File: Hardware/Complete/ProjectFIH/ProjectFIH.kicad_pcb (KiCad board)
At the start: 2 copper layers, 94 x 99.1 mm, 84 parts, among them J1 Conn_01x02_Male, J10 Payload LED, J2 Power, J3 Power LED, J4 MCU Fail LED, J5 Heater LED, J6 Heater, J7 UART, J8 AVR-ISP-10, J9 Payload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

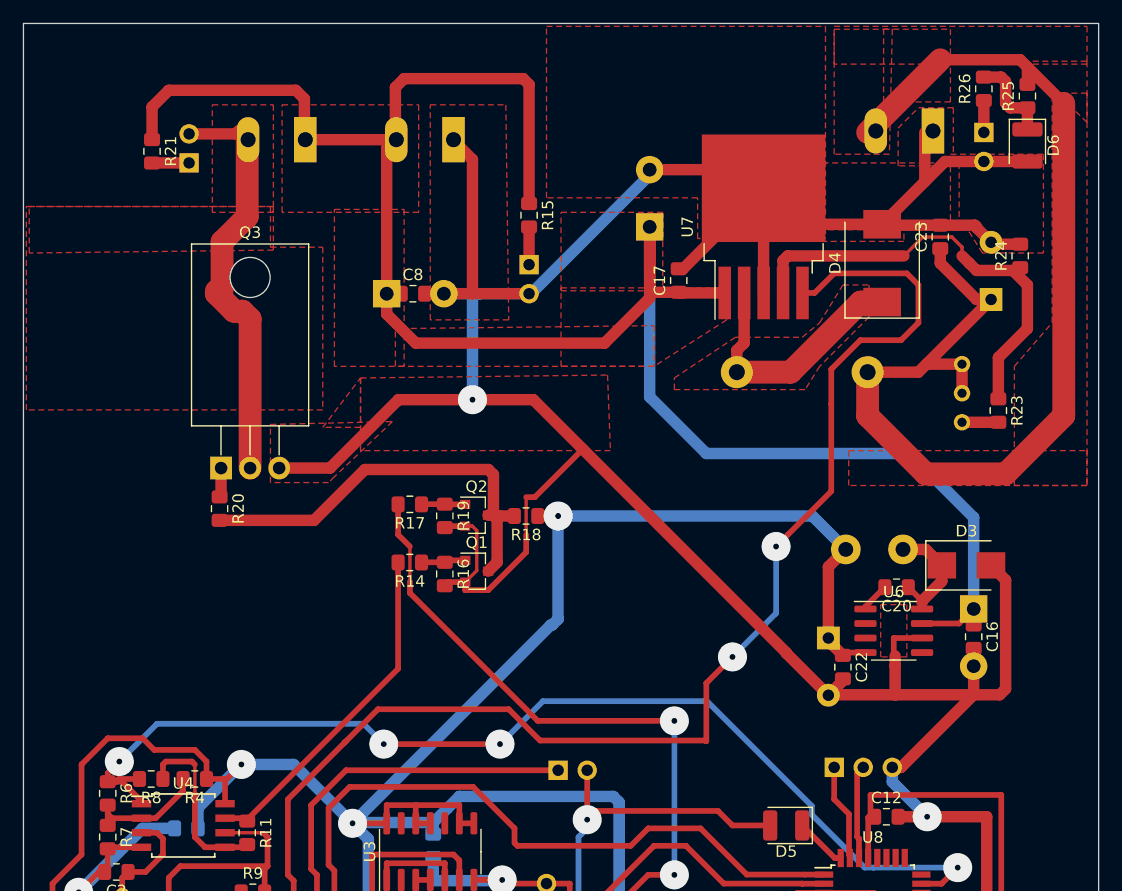
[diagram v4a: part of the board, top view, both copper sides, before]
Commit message: Partially metallized empty spaces.
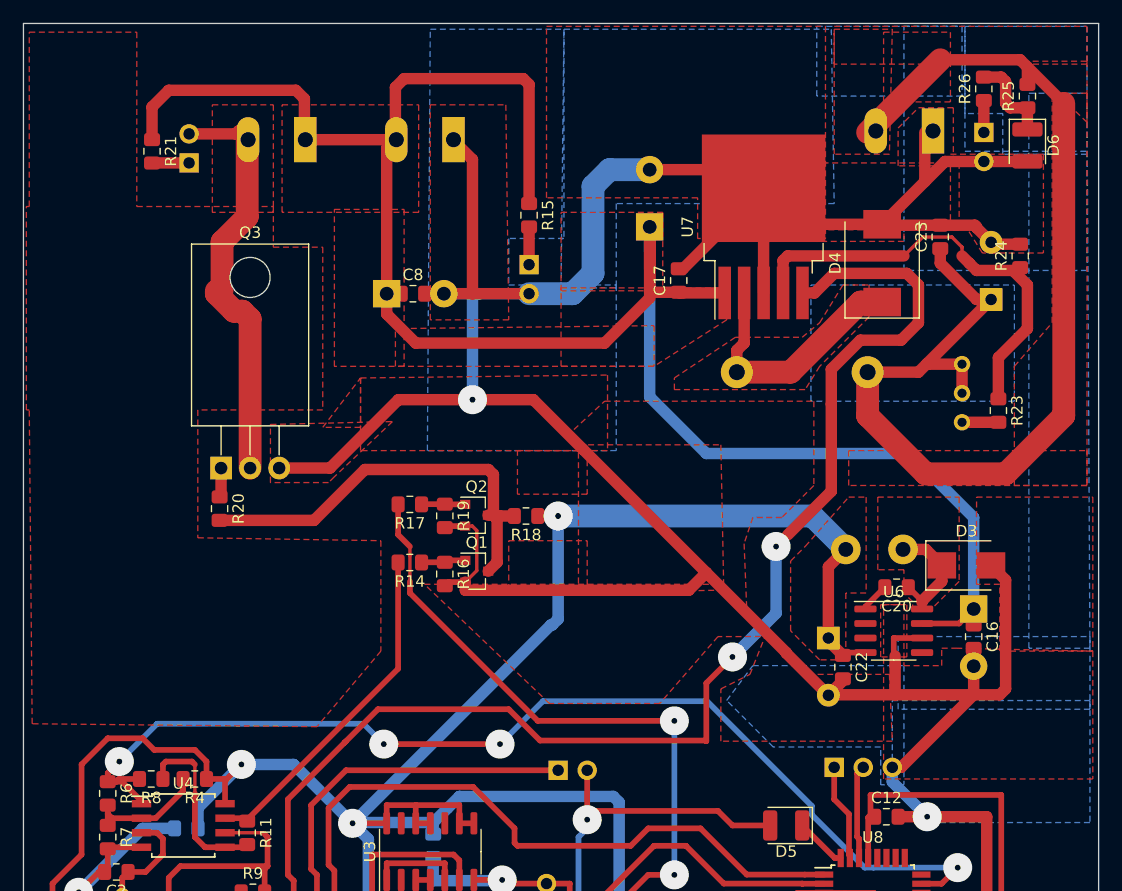
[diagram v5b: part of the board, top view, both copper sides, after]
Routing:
- net GND: track 532.7 -> 541.1 mm
- net +24V: track 178.7 -> 180.8 mm
- added copper zone on F.Cu, net +5V
- added copper zone on B.Cu, net GND
- added copper zone on F.Cu, net Net-(C20-Pad1)
- added copper zone on B.Cu, net Net-(C23-Pad1)

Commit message: Most of metallization
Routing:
- added copper zone on B.Cu, net +24V
- added copper zone on B.Cu, net +5V
- added copper zone on B.Cu, net Net-(J5-Pad2)

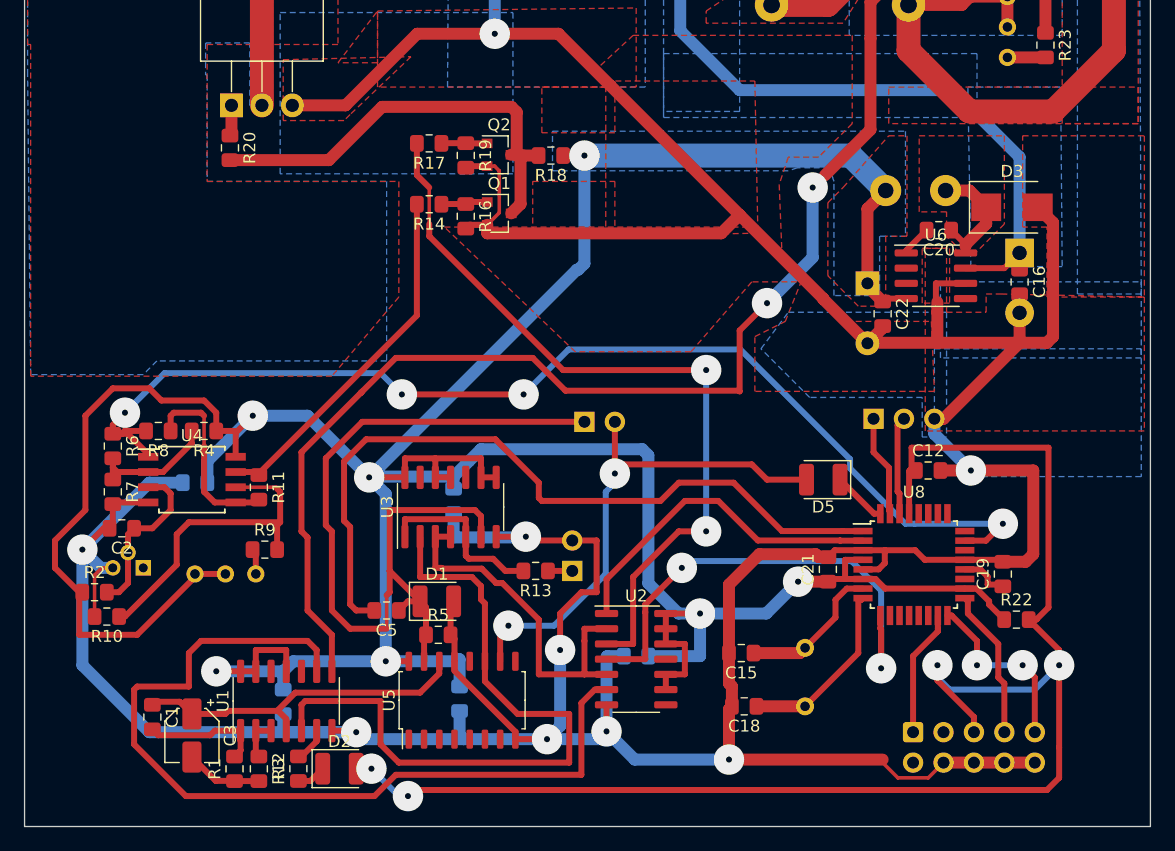
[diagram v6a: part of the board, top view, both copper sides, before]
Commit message: Filled. Imperfect, but don't want to re-do.
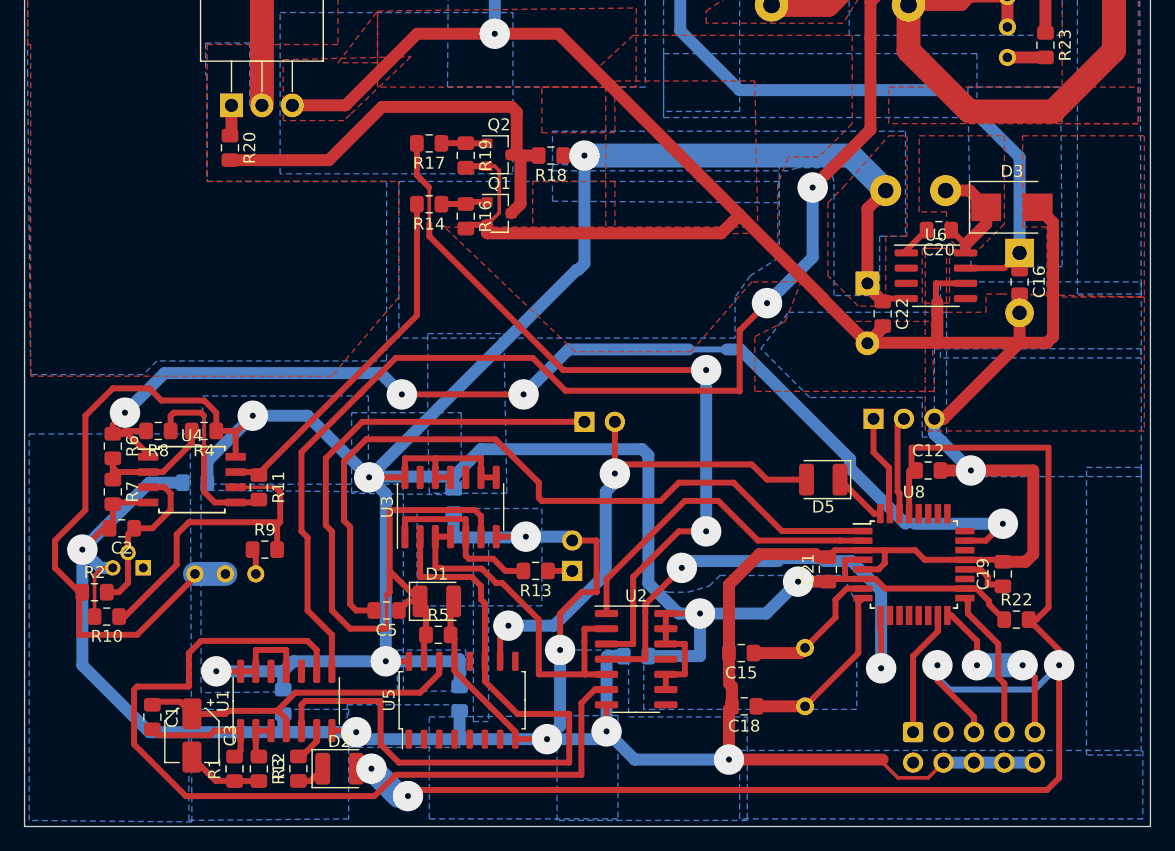
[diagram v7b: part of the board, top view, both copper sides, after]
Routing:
- net MCU_PL_ON: track 40.9 -> 43.2 mm
- net Temperature: track 95.4 -> 96.5 mm
